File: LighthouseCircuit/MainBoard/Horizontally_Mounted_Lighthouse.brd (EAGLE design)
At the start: 25.4 x 10.2 mm, 23 parts

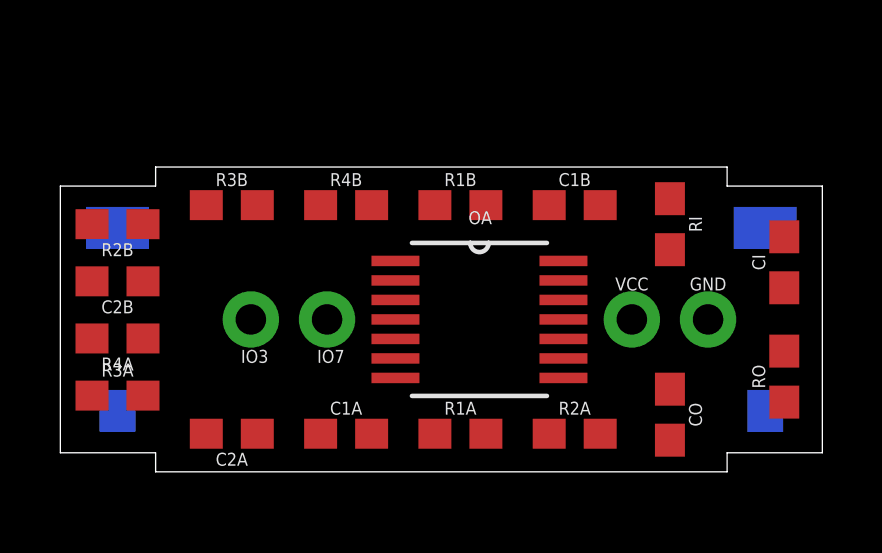
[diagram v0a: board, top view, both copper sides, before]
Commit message: Progress toward using bi-arc computations for execution of path following.
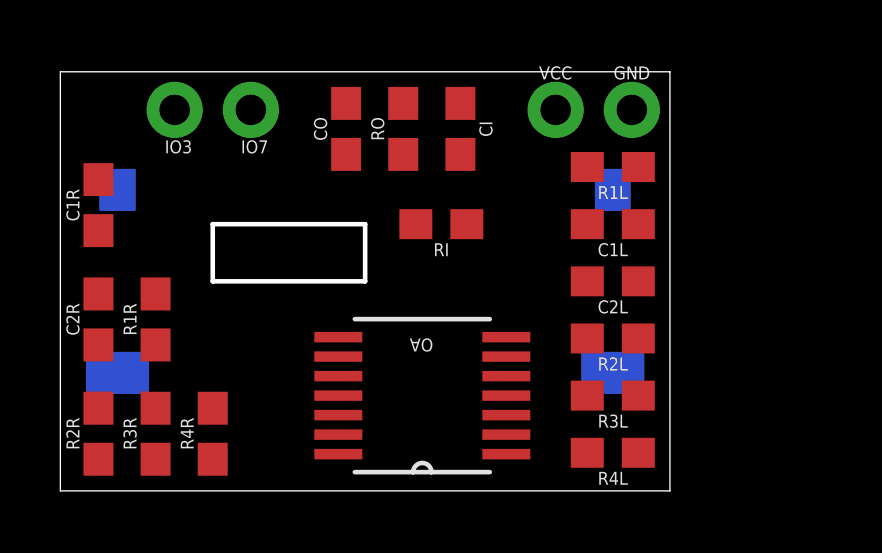
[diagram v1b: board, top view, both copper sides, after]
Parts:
- removed C1A, C1B: 5pF, ZippyComponentLibrary:PASSIVE-0603
- removed C2A, C2B: 4.7nF, ZippyComponentLibrary:PASSIVE-0603
- removed D1, D2: PHOTODIODEBPW, ZippyComponentLibrary:BPW34_BP104_SMD
- removed R1A, R1B: 120k, ZippyComponentLibrary:PASSIVE-0603
- removed R2A, R2B: 18k, ZippyComponentLibrary:PASSIVE-0603
- removed R3A: 1K, ZippyComponentLibrary:PASSIVE-0603
- removed R3B: 1k, ZippyComponentLibrary:PASSIVE-0603
- removed R4A, R4B: 100k, ZippyComponentLibrary:PASSIVE-0603
- added C1L, C1R: 5pF, ZippyComponentLibrary:PASSIVE-0603
- added C2L, C2R: 4.7nF, ZippyComponentLibrary:PASSIVE-0603
- added DL, DR: PHOTODIODEBPW, ZippyComponentLibrary:BPW34_BP104_SMD
- added R1L, R1R, R4L, R4R: 100k, ZippyComponentLibrary:PASSIVE-0603
- added R2L, R2R: 18k, ZippyComponentLibrary:PASSIVE-0603
- added R3L: 1k, ZippyComponentLibrary:PASSIVE-0603
- added R3R: 1K, ZippyComponentLibrary:PASSIVE-0603
- moved RO 15.1 mm to (11.4, 12.1)
- moved CO 14.4 mm to (9.53, 12.1), turned to 90 degrees
- moved CI 11.7 mm to (13.3, 12.1), turned to 90 degrees
- moved RI 7.62 mm to (12.7, 8.89), turned to 180 degrees
- moved GND 7.43 mm to (19.1, 12.7)
- moved IO3 7.43 mm to (3.81, 12.7)
- moved IO7 7.43 mm to (6.35, 12.7)
- moved VCC 7.43 mm to (16.5, 12.7)
- moved OA 3.18 mm to (12.1, 3.17), turned to 180 degrees
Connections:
- removed net D1IN: C1B.1, D2.CATHODE, OA.13, R1B.1
- removed net D1OA2P: C2B.2, OA.2, R2B.1
- removed net D1OAOUT1: C1B.2, C2B.1, OA.14, R1B.2
- removed net D2IN: C1A.1, D1.CATHODE, OA.9, R1A.1
- removed net D2OA1OUT: C1A.2, C2A.1, OA.8, R1A.2
- removed net D2OA2N: OA.5, R3A.1, R4A.1
- removed net D2OA2P: C2A.2, OA.6, R2A.1
- removed net N$11: OA.3, R3B.1, R4B.1
- new net DL1IN: C1L.1, DL.CATHODE, OA.6, R1L.1
- new net DL1OUT: C1L.2, C2L.1, OA.7, R1L.2
- new net DL2F: OA.3, R3L.1, R4L.1
- new net DL2IN: C2L.2, OA.2, R2L.1
- new net DR1IN: C1R.1, DR.CATHODE, OA.13, R1R.1
- new net DR1OUT: C1R.2, C2R.1, OA.14, R1R.2
- new net DR2F: OA.10, R3R.1, R4R.1
- new net DR2IN: C2R.2, OA.9, R2R.1
- net IO3: now also OA.8, R4R.2; no longer OA.7, R4A.2
- net IO7: now also R4L.2; no longer R4B.2
- net LVCC: now also DL.ANODE, DR.ANODE, OA.5, R2L.2, R2R.2, R3L.2, R3R.2; no longer D1.ANODE, D2.ANODE, OA.10, R2A.2, R2B.2, R3A.2, R3B.2
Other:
- board size 25.4 x 10.2 mm -> 20.3 x 14 mm
